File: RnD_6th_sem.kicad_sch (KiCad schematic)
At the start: 47 parts, among them J1 HVDC1, J2 PWM, J3 HVDC2, Q1 IGLD60R190D1, Q2 IGLD60R190D1, U1 2EDF7275K

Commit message: updated the schematic
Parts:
- removed C12: 100uF/250V, symbol Device:C_Polarized
- removed D3, D4: D_Schottky, Diode_THT:D_5KPW_P12.70mm_Horizontal, symbol Device:D_Schottky
- removed FB1, FB2: fb, Resistor_SMD:R_0805_2012Metric, symbol Device:FerriteBead_Small
- removed R?: R_SENSE, symbol Device:R_US
- added H1, H2, H3, H4: MountingHole, symbol Mechanical:MountingHole
- added J4: 3.3V, Connector_Molex:Molex_KK-254_AE-6410-02A_1x02_P2.54mm_Vertical, symbol Connector:Conn_01x02_Male
- added J5, J6: 5V, symbol Connector:Conn_01x02_Male
- added J7: GND2, symbol Connector:Conn_01x02_Male
- added J8: GND1, symbol Connector:Conn_01x02_Male
- added R17, R18, R19, R20: 1R, symbol Device:R
- added R21, R22: NC, symbol Device:R
- added R8: 500k, symbol Device:R
- added R9: WSLP3921L1000FEA, footprint:RESC10052X50N, symbol WSLP3921L1000FEA:WSLP3921L1000FEA
- added U2, U3: LS05, symbol DC-DC Powersupply:LS05
- C10: value 100uF/250V -> 220uF/450V; footprint (none) -> Capacitor_SMD:CP_Elec_4x5.8
- C15, C16: footprint (none) -> Capacitor_SMD:CP_Elec_4x5.8
- C6, C7: value 100nF/100V -> 100nF/630V; footprint Capacitor_SMD:C_0805_2012Metric -> (none)
- C8, C9: value 100nF/100V -> 1uF/450V; footprint Capacitor_SMD:C_0805_2012Metric -> (none)
- R7: renamed from R?; footprint RESC10052X50N -> footprint:RESC10052X50N
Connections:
- net +3.3V: now also J4.1 (Pin_1)
- net GND: now also J4.2 (Pin_2)
- net VCCA: now also FB4.2, R11.2, J5.1 (Pin_1); no longer C15.1, C2.2, FB3.2, R12.2
- net VCCB: now also FB3.2, R12.2, J6.2 (Pin_2); no longer C16.1, C3.2, FB4.2, R11.2
- net HVDC+: now reaches C10.1, J1.3 (Pin_3), J3.3 (Pin_3), R7.2
- net HVDC+: now also C6.1, C7.1, C8.1, C9.1, R8.1, U2.1 (IN+), U3.1 (IN+); no longer C8.2, C9.2
- net at U1.11 (GNDA): now also C15.2, C2.1, J8.2 (Pin_2)
- net GND3: now reaches C7.2
- net GND3: now also C10.2, C6.2, C8.2, C9.2, J1.2 (Pin_2), J3.2 (Pin_2), R8.2, R9.2, U2.2 (IN-), U3.2 (IN-); no longer C9.1
- net at U1.13 (VCCA): now also C15.1, C2.2, J5.2 (Pin_2); no longer FB3.1
- net at U1.8 (GNDB): now also C16.2, C3.1, J7.1 (Pin_1)
- net at FB4.1: now also U2.3 (5V); no longer U1.10 (VCCB)
- removed net GNDA: C15.2, C2.1, D7.1 (K), Q1.7 (SS)
- removed net GNDB: C16.2, C3.1, D6.1 (K), Q2.7 (SS)
- net OUTAB renamed OUTB
- net pwm1 renamed PWM1
- net pwm2 renamed PWM2
- new net: Q2.5 (S), Q2.6 (S), Q2.9 (S), R17.1, R18.1, R19.1, R20.1, R21.1, R22.1
- new net: R17.2, R18.2, R19.2, R20.2, R21.2, R22.2, R9.1
- new net: C16.1, C3.2, J6.1 (Pin_1), U1.10 (VCCB)
- new net: FB3.1, U3.3 (5V)
- new net GND1: D6.1 (K), J8.1 (Pin_1), Q1.7 (SS), U2.4 (GND)
- new net GND2: D7.1 (K), J7.2 (Pin_2), Q2.7 (SS), U3.4 (GND)
- no-connect marks 1 -> 5
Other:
- note added: "Gate Driver Circuit"
- note added: "ISOLATED 5V DC"
- note added: "LEDs"
- note added: "PWM RC Filter"
- moved on the sheet: C1, C13, C14, C15, C16, C2, C3, C4, C5, D1, D2, D5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

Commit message: after ubuntu push
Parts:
- R17, R18, R19, R20, R21, R22, R8: footprint (none) -> Resistor_SMD:R_0805_2012Metric
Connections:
- net PWM1: now also C14.2, R14.2, R16.1; no longer C13.2, R13.2, R15.1
- net PWM2: now also C13.2, R13.2, R15.1; no longer C14.2, R14.2, R16.1
- net VCCA: no longer R11.2
- net VCCB: no longer R12.2
- net LED1: now reaches C15.1, C2.2, J5.2 (Pin_2), U1.13 (VCCA)
- net LED1: now also R11.2
- net LED2: now reaches C16.1, C3.2, J6.1 (Pin_1), U1.10 (VCCB)
- net LED2: now also R12.2
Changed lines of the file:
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@@
   (junction (at 132.08 154.305) (diameter 0) (color 0 0 0 0)
   )
+  (junction (at 95.25 92.075) (diameter 0) (color 0 0 0 0)
+  )
   (junction (at 37.465 36.83) (diameter 0) (color 0 0 0 0)
   )
@@
   )
   (junction (at 247.015 33.02) (diameter 0) (color 0 0 0 0)
-  )
-  (junction (at 95.25 92.075) (diameter 0) (color 0 0 0 0)
   )
   (junction (at 132.08 146.685) (diameter 0) (color 0 0 0 0)
@@
     (stroke (width 0) (type default) (color 0 0 0 0))
   )
-  (wire (pts (xy 46.99 22.86) (xy 48.895 22.86))
-    (stroke (width 0) (type default) (color 0 0 0 0))
-  )
   (wire (pts (xy 164.465 93.98) (xy 172.085 93.98))
     (stroke (width 0) (type default) (color 0 0 0 0))
@@
     (stroke (width 0) (type default) (color 0 0 0 0))
   )
+  (wire (pts (xy 187.325 24.765) (xy 187.325 27.305))
+    (stroke (width 0) (type default) (color 0 0 0 0))
+  )
   (wire (pts (xy 212.725 104.775) (xy 212.725 99.695))
     (stroke (width 0) (type default) (color 0 0 0 0))
@@
     (stroke (width 0) (type default) (color 0 0 0 0))
   )
-  (wire (pts (xy 46.99 54.61) (xy 48.895 54.61))
+  (wire (pts (xy 46.99 54.61) (xy 49.53 54.61))
+    (stroke (width 0) (type default) (color 0 0 0 0))
+  )
+  (wire (pts (xy 46.99 22.86) (xy 50.8 22.86))
     (stroke (width 0) (type default) (color 0 0 0 0))
   )
@@
   )
   (wire (pts (xy 264.795 48.26) (xy 270.51 48.26))
+    (stroke (width 0) (type default) (color 0 0 0 0))
+  )
+  (wire (pts (xy 184.15 40.64) (xy 184.15 42.545))
     (stroke (width 0) (type default) (color 0 0 0 0))
   )
@@
     )
   )
+  (global_label "LED1" (shape input) (at 187.325 24.765 90) (fields_autoplaced)
+    (effects (font (size 1 1)) (justify left))
+    (property "Intersheet References" "${INTERSHEET_REFS}" (id 0) (at 187.2625 19.1983 90)
+      (effects (font (size 1 1)) (justify left) hide)
+    )
+  )
   (global_label "VCCB" (shape input) (at 277.495 48.26 0) (fields_autoplaced)
     (effects (font (size 1 1)) (justify left))
@@
     )
   )
-  (global_label "PWM1" (shape input) (at 48.895 22.86 0) (fields_autoplaced)
+  (global_label "PWM1" (shape input) (at 49.53 54.61 0) (fields_autoplaced)
     (effects (font (size 1.27 1.27)) (justify left))
-    (property "Intersheet References" "${INTERSHEET_REFS}" (id 0) (at 56.6905 22.7806 0)
-      (effects (font (size 1.27 1.27)) (justify left) hide)
-    )
-  )
-  (global_label "PWM2" (shape input) (at 48.895 54.61 0) (fields_autoplaced)
+    (property "Intersheet References" "${INTERSHEET_REFS}" (id 0) (at 57.3255 54.5306 0)
+      (effects (font (size 1.27 1.27)) (justify left) hide)
+    )
+  )
+  (global_label "PWM2" (shape input) (at 50.8 22.86 0) (fields_autoplaced)
     (effects (font (size 1.27 1.27)) (justify left))
-    (property "Intersheet References" "${INTERSHEET_REFS}" (id 0) (at 56.6905 54.5306 0)
-      (effects (font (size 1.27 1.27)) (justify left) hide)
-    )
-  )
-  (global_label "VCCA" (shape input) (at 35.56 80.645 90) (fields_autoplaced)
-    (effects (font (size 1 1)) (justify left))
-    (property "Intersheet References" "${INTERSHEET_REFS}" (id 0) (at 35.4975 75.0307 90)
-      (effects (font (size 1 1)) (justify left) hide)
+    (property "Intersheet References" "${INTERSHEET_REFS}" (id 0) (at 58.5955 22.7806 0)
+      (effects (font (size 1.27 1.27)) (justify left) hide)
     )
   )
@@
     )
   )
+  (global_label "LED2" (shape input) (at 184.15 40.64 0) (fields_autoplaced)
+    (effects (font (size 1 1)) (justify left))
+    (property "Intersheet References" "${INTERSHEET_REFS}" (id 0) (at 189.7167 40.5775 0)
+      (effects (font (size 1 1)) (justify left) hide)
+    )
+  )
+  (global_label "LED2" (shape input) (at 45.085 80.645 90) (fields_autoplaced)
+    (effects (font (size 1 1)) (justify left))
+    (property "Intersheet References" "${INTERSHEET_REFS}" (id 0) (at 45.0225 75.0783 90)
+      (effects (font (size 1 1)) (justify left) hide)
+    )
+  )
   (global_label "OUTA" (shape input) (at 87.63 102.87 270) (fields_autoplaced)
     (effects (font (size 0.7 0.7)) (justify right))
@@
     )
   )
-  (global_label "VCCB" (shape input) (at 45.085 80.645 90) (fields_autoplaced)
-    (effects (font (size 1 1)) (justify left))
-    (property "Intersheet References" "${INTERSHEET_REFS}" (id 0) (at 45.0225 74.8879 90)
-      (effects (font (size 1 1)) (justify left) hide)
-    )
-  )
   (global_label "OUTB" (shape input) (at 88.265 123.19 90) (fields_autoplaced)
     (effects (font (size 0.7 0.7)) (justify left))
@@
     )
   )
+  (global_label "LED1" (shape input) (at 35.56 80.645 90) (fields_autoplaced)
+    (effects (font (size 1 1)) (justify left))
+    (property "Intersheet References" "${INTERSHEET_REFS}" (id 0) (at 35.4975 75.0783 90)
+      (effects (font (size 1 1)) (justify left) hide)
+    )
+  )
   (global_label "HVDC+" (shape input) (at 242.57 33.02 180) (fields_autoplaced)
     (effects (font (size 1.27 1.27)) (justify right))
@@
       (effects (font (size 1 1)) (justify left))
     )
-    (property "Footprint" "" (id 2) (at 122.047 150.495 90)
+    (property "Footprint" "Resistor_SMD:R_0805_2012Metric" (id 2) (at 122.047 150.495 90)
       (effects (font (size 1.27 1.27)) hide)
     )
@@
       (effects (font (size 1 1)) (justify left))
     )
-    (property "Footprint" "" (id 2) (at 253.492 95.885 90)
+    (property "Footprint" "Resistor_SMD:R_0805_2012Metric" (id 2) (at 253.492 95.885 90)
       (effects (font (size 1.27 1.27)) hide)
     )
@@
       (effects (font (size 1 1)) (justify left))
     )
-    (property "Footprint" "" (id 2) (at 144.272 150.495 90)
+    (property "Footprint" "Resistor_SMD:R_0805_2012Metric" (id 2) (at 144.272 150.495 90)
       (effects (font (size 1.27 1.27)) hide)
     )
@@
       (effects (font (size 1 1)) (justify left))
     )
-    (property "Footprint" "" (id 2) (at 127.762 150.495 90)
+    (property "Footprint" "Resistor_SMD:R_0805_2012Metric" (id 2) (at 127.762 150.495 90)
       (effects (font (size 1.27 1.27)) hide)
     )
@@
       (effects (font (size 1 1)) (justify left))
     )
-    (property "Footprint" "" (id 2) (at 133.477 150.495 90)
+    (property "Footprint" "Resistor_SMD:R_0805_2012Metric" (id 2) (at 133.477 150.495 90)
       (effects (font (size 1.27 1.27)) hide)
     )
@@
       (effects (font (size 1 1)) (justify left))
     )
-    (property "Footprint" "" (id 2) (at 115.697 150.495 90)
+    (property "Footprint" "Resistor_SMD:R_0805_2012Metric" (id 2) (at 115.697 150.495 90)
       (effects (font (size 1.27 1.27)) hide)
     )
@@
       (effects (font (size 1 1)) (justify left))
     )
-    (property "Footprint" "" (id 2) (at 138.557 150.495 90)
+    (property "Footprint" "Resistor_SMD:R_0805_2012Metric" (id 2) (at 138.557 150.495 90)
       (effects (font (size 1.27 1.27)) hide)
     )
@@
     )
     (path "/544a4d40-b61f-4efe-a98d-bd770de85966"
-      (reference "R8") (unit 1) (value "500k") (footprint "")
+      (reference "R8") (unit 1) (value "500k") (footprint "Resistor_SMD:R_0805_2012Metric")
     )
     (path "/8ab46d10-f250-46a4-ab4f-73b7a7aef8c7"
@@
     )
     (path "/e81249f0-7eae-43dc-a9f4-4d9431b6af46"
-      (reference "R17") (unit 1) (value "1R") (footprint "")
+      (reference "R17") (unit 1) (value "1R") (footprint "Resistor_SMD:R_0805_2012Metric")
     )
     (path "/1ec36f99-3629-41de-ae8f-86fda3acbc1d"
-      (reference "R18") (unit 1) (value "1R") (footprint "")
+      (reference "R18") (unit 1) (value "1R") (footprint "Resistor_SMD:R_0805_2012Metric")
     )
     (path "/b06bb4d3-7fd5-4e6b-8fcf-a360994a4e63"
-      (reference "R19") (unit 1) (value "1R") (footprint "")
+      (reference "R19") (unit 1) (value "1R") (footprint "Resistor_SMD:R_0805_2012Metric")
     )
     (path "/c6376ad3-e623-4f28-871a-69ce253cf749"
-      (reference "R20") (unit 1) (value "1R") (footprint "")
+      (reference "R20") (unit 1) (value "1R") (footprint "Resistor_SMD:R_0805_2012Metric")
     )
     (path "/fcd152ec-0e3a-4f89-946a-25db7a726d2c"
-      (reference "R21") (unit 1) (value "NC") (footprint "")
+      (reference "R21") (unit 1) (value "NC") (footprint "Resistor_SMD:R_0805_2012Metric")
     )
     (path "/998b7076-7f3b-49a0-9a7f-efeeea90d732"
-      (reference "R22") (unit 1) (value "NC") (footprint "")
+      (reference "R22") (unit 1) (value "NC") (footprint "Resistor_SMD:R_0805_2012Metric")
     )
     (path "/929a0c5a-85ce-4abc-b13f-988818069efe"

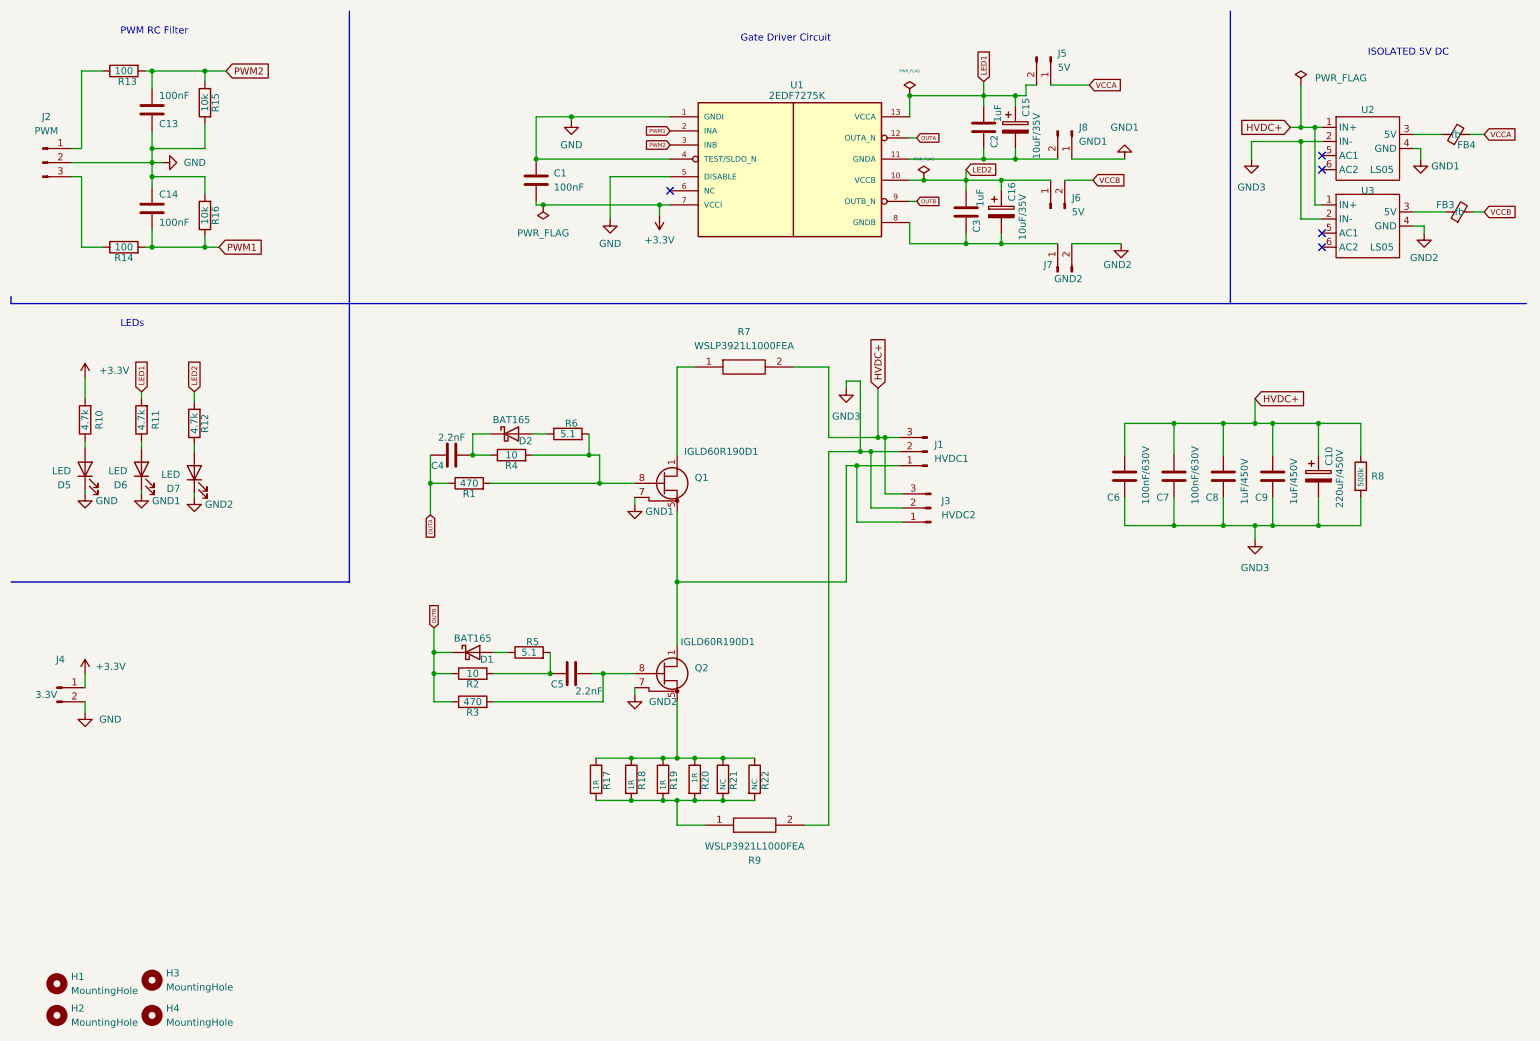
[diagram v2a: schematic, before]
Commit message: changed GD Symbol
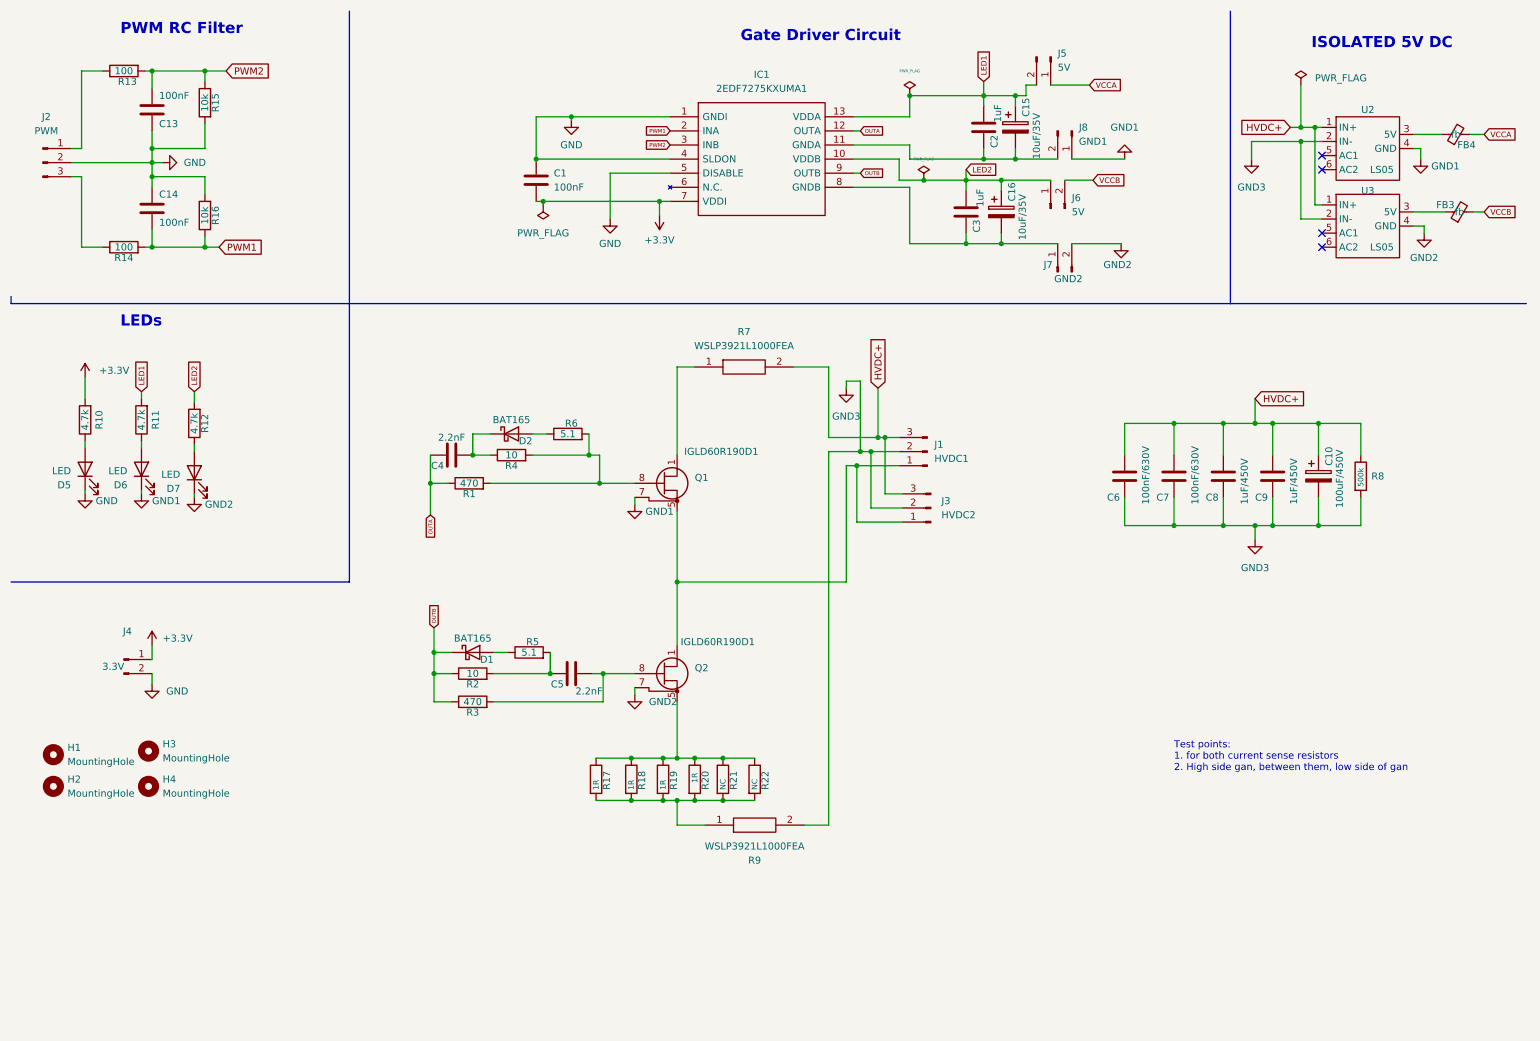
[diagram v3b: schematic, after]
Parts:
- removed U1: 2EDF7275K, footprint:TFLGA65P500X500X106-14_13N-V, symbol 2EDF7275K:2EDF7275K
- added IC1: 2EDF7275KXUMA1, 2EDF7275KXUMA1:2EDF7275KXUMA1, symbol 2EDF7275KXUMA1:2EDF7275KXUMA1
- C10: value 220uF/450V -> 100uF/450V; footprint Capacitor_SMD:CP_Elec_4x5.8 -> Capacitor_THT:CP_Radial_D18.0mm_P7.50mm
- C6, C7: footprint (none) -> Capacitor_SMD:C_1206_3216Metric
- C8, C9: footprint (none) -> CGA9P4X7T2W105K250KA:CAPC5750X280N
- H1, H2, H3, H4: footprint (none) -> MountingHole:MountingHole_3.2mm_M3
- J5, J6, J7, J8: footprint (none) -> Connector_PinHeader_2.54mm:PinHeader_1x02_P2.54mm_Vertical
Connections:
- net +3.3V: now also IC1.7 (VDDI)
- net GND: now also IC1.1 (GNDI), IC1.4 (SLDON), IC1.5 (DISABLE)
- net LED1: now also IC1.13 (VDDA)
- net LED2: now also IC1.10 (VDDB)
- net OUTA: now also IC1.12 (OUTA)
- net OUTB: now also IC1.9 (OUTB)
- net PWM1: now also IC1.2 (INA)
- net PWM2: now also IC1.3 (INB)
- net at C15.2, C2.1, J8.2 (Pin_2): now also IC1.11 (GNDA)
- net at C16.2, C3.1, J7.1 (Pin_1): now also IC1.8 (GNDB)
- no-connect marks 5 -> 4
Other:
- note added: "Test points: 1. for both current sense resistors 2. High side gan, between them, low side of gan"
- moved on the sheet: H1, H2, H3, H4, J4
